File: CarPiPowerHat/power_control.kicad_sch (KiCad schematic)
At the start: 21 parts, among them U3 LM3480-5.0, U4 ATtiny45V-10X

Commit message: updated layout
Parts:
- D5: footprint Diode_SMD:D_0603_1608Metric_Pad1.05x0.95mm_HandSolder -> Diode_SMD:D_SMA_Handsoldering
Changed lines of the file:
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@@
-(kicad_sch (version 20210126) (generator eeschema)
+(kicad_sch (version 20210406) (generator eeschema)
   (paper "A4")
   (junction (at 41.91 43.815) (diameter 1.016) (color 0 0 0 0))
@@
       (effects (font (size 1.27 1.27)) (justify right))
     )
-    (property "Footprint" "Diode_SMD:D_0603_1608Metric_Pad1.05x0.95mm_HandSolder" (id 2) (at 41.91 50.165 0)
-      (effects (font (size 1.27 1.27)) hide)
-    )
+    (property "Footprint" "Diode_SMD:D_SMA_Handsoldering" (id 2) (at 41.91 50.165 0)
+      (effects (font (size 1.27 1.27)) hide)
+    )

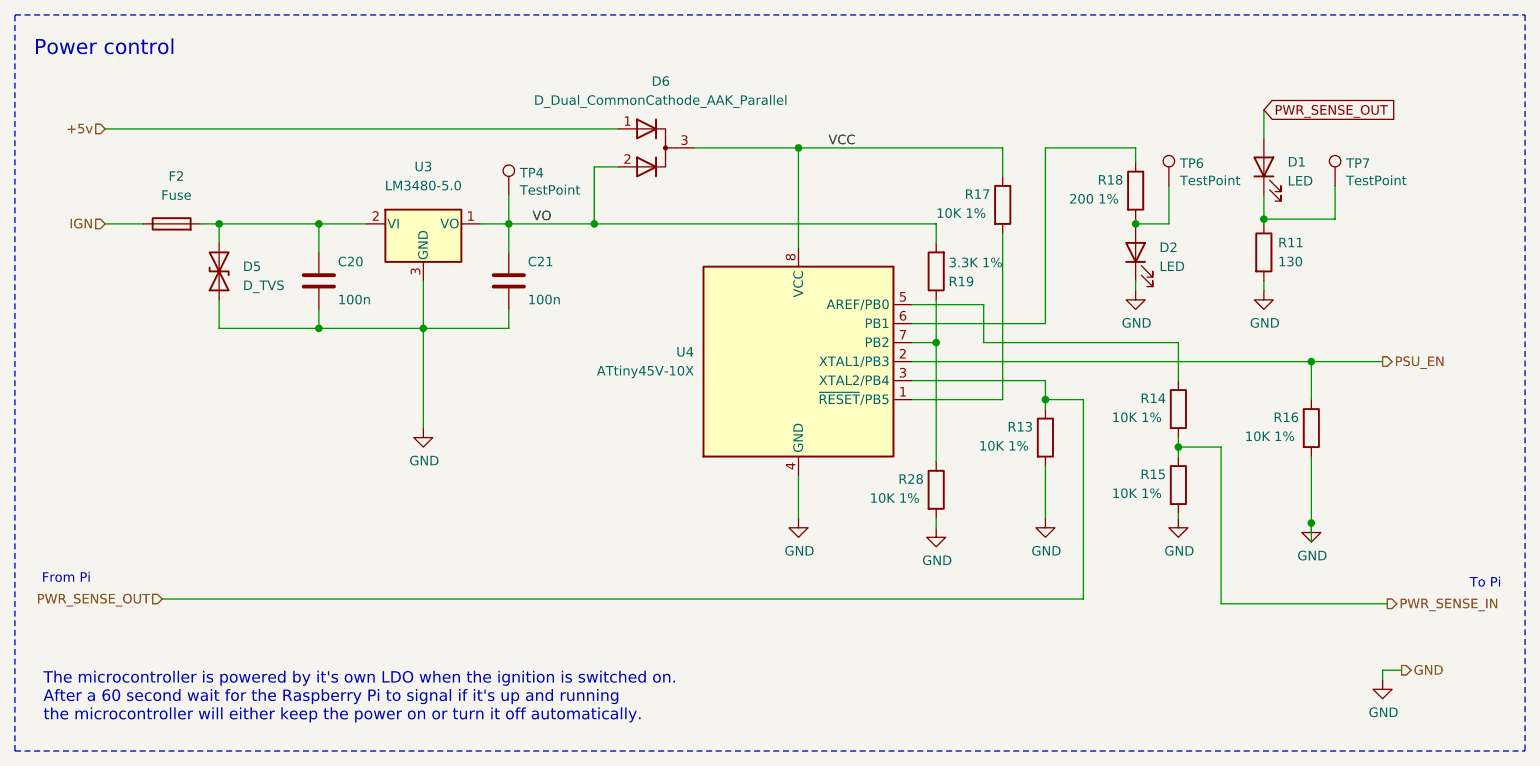
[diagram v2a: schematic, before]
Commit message: Removed TVS diodes for now, fixed DRC issues
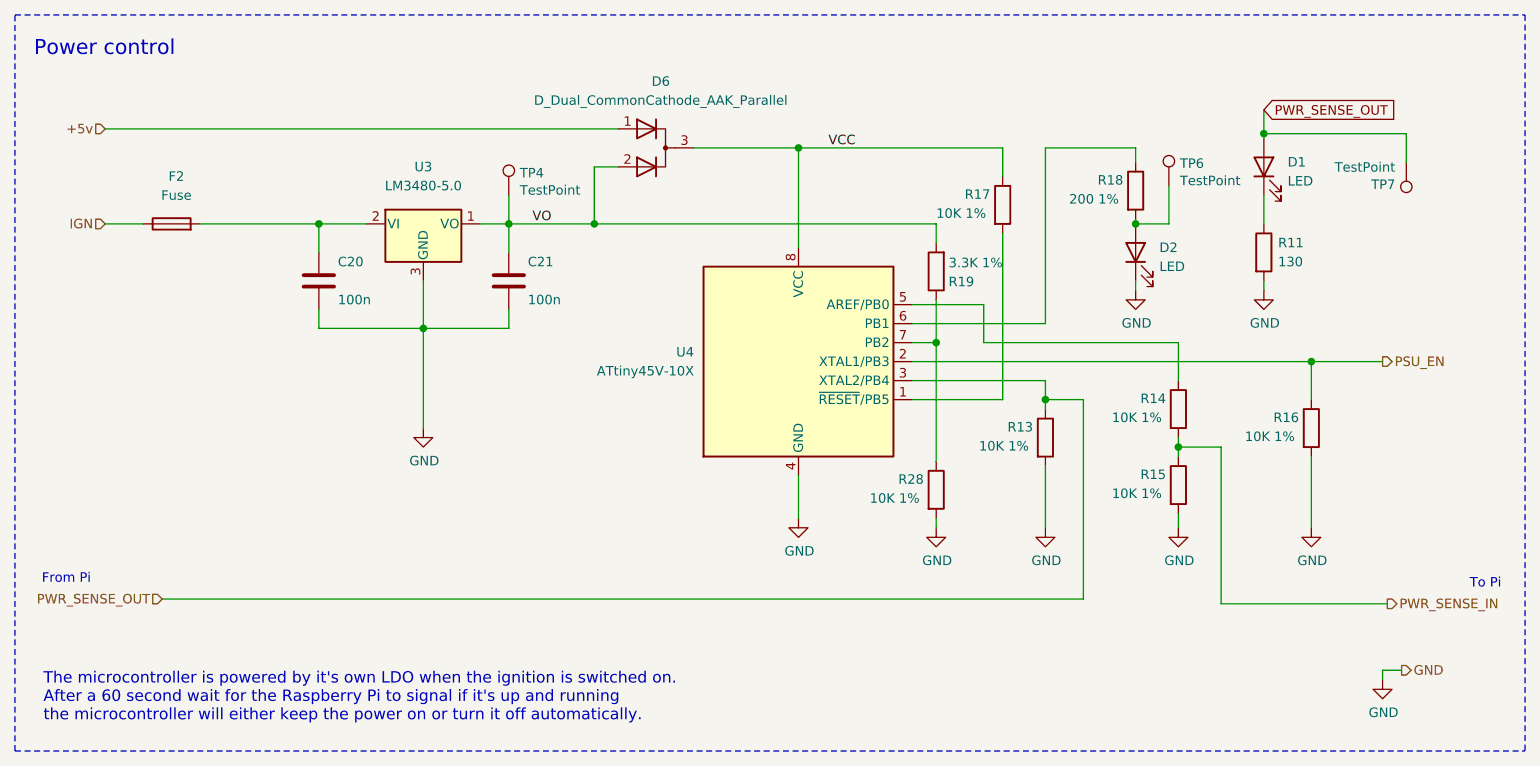
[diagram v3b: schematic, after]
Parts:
- removed D5: D_TVS, Diode_SMD:D_SMA_Handsoldering, symbol Device:D_TVS
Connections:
- net PWR_SENSE_OUT: now also TP7.1
- net at D1.1 (K), R11.1: no longer TP7.1
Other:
- moved on the sheet: TP7
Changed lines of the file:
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@@
 (kicad_sch (version 20210621) (generator eeschema)
   (paper "A4")
-  (junction (at 41.91 43.815) (diameter 1.016) (color 0 0 0 0))
   (junction (at 55.245 43.815) (diameter 1.016) (color 0 0 0 0))
-  (junction (at 55.245 57.785) (diameter 1.016) (color 0 0 0 0))
   (junction (at 69.215 57.785) (diameter 1.016) (color 0 0 0 0))
   (junction (at 80.645 43.815) (diameter 1.016) (color 0 0 0 0))
@@
   (junction (at 164.465 43.815) (diameter 1.016) (color 0 0 0 0))
   (junction (at 170.18 73.66) (diameter 1.016) (color 0 0 0 0))
-  (junction (at 181.61 43.18) (diameter 1.016) (color 0 0 0 0))
+  (junction (at 181.61 31.75) (diameter 1.016) (color 0 0 0 0))
   (junction (at 187.96 62.23) (diameter 1.016) (color 0 0 0 0))
-  (junction (at 187.96 83.82) (diameter 1.016) (color 0 0 0 0))
   (wire (pts (xy 26.67 31.115) (xy 95.25 31.115))
     (stroke (width 0) (type solid) (color 0 0 0 0))
@@
     (stroke (width 0) (type solid) (color 0 0 0 0))
   )
-  (wire (pts (xy 39.37 43.815) (xy 41.91 43.815))
-    (stroke (width 0) (type solid) (color 0 0 0 0))
-  )
-  (wire (pts (xy 41.91 43.815) (xy 41.91 46.355))
-    (stroke (width 0) (type solid) (color 0 0 0 0))
-  )
-  (wire (pts (xy 41.91 43.815) (xy 55.245 43.815))
-    (stroke (width 0) (type solid) (color 0 0 0 0))
-  )
-  (wire (pts (xy 41.91 53.975) (xy 41.91 57.785))
-    (stroke (width 0) (type solid) (color 0 0 0 0))
-  )
-  (wire (pts (xy 41.91 57.785) (xy 55.245 57.785))
+  (wire (pts (xy 39.37 43.815) (xy 55.245 43.815))
     (stroke (width 0) (type solid) (color 0 0 0 0))
   )
@@
     (stroke (width 0) (type solid) (color 0 0 0 0))
   )
-  (wire (pts (xy 152.4 76.2) (xy 152.4 83.185))
+  (wire (pts (xy 152.4 76.2) (xy 152.4 84.455))
     (stroke (width 0) (type solid) (color 0 0 0 0))
   )
@@
     (stroke (width 0) (type solid) (color 0 0 0 0))
   )
-  (wire (pts (xy 170.18 82.55) (xy 170.18 83.185))
+  (wire (pts (xy 170.18 82.55) (xy 170.18 84.455))
     (stroke (width 0) (type solid) (color 0 0 0 0))
   )
@@
     (stroke (width 0) (type solid) (color 0 0 0 0))
   )
-  (wire (pts (xy 181.61 28.575) (xy 181.61 32.385))
-    (stroke (width 0) (type solid) (color 0 0 0 0))
-  )
-  (wire (pts (xy 181.61 40.005) (xy 181.61 43.18))
-    (stroke (width 0) (type solid) (color 0 0 0 0))
-  )
-  (wire (pts (xy 181.61 43.18) (xy 181.61 43.815))
+  (wire (pts (xy 181.61 28.575) (xy 181.61 31.75))
+    (stroke (width 0) (type solid) (color 0 0 0 0))
+  )
+  (wire (pts (xy 181.61 31.75) (xy 181.61 32.385))
+    (stroke (width 0) (type solid) (color 0 0 0 0))
+  )
+  (wire (pts (xy 181.61 31.75) (xy 200.66 31.75))
+    (stroke (width 0) (type solid) (color 0 0 0 0))
+  )
+  (wire (pts (xy 181.61 40.005) (xy 181.61 43.815))
     (stroke (width 0) (type solid) (color 0 0 0 0))
   )
@@
     (stroke (width 0) (type solid) (color 0 0 0 0))
   )
-  (wire (pts (xy 187.96 74.93) (xy 187.96 83.82))
-    (stroke (width 0) (type solid) (color 0 0 0 0))
-  )
-  (wire (pts (xy 187.96 86.36) (xy 187.96 83.82))
-    (stroke (width 0) (type solid) (color 0 0 0 0))
-  )
-  (wire (pts (xy 191.135 38.735) (xy 191.135 43.18))
-    (stroke (width 0) (type solid) (color 0 0 0 0))
-  )
-  (wire (pts (xy 191.135 43.18) (xy 181.61 43.18))
+  (wire (pts (xy 187.96 74.93) (xy 187.96 84.455))
     (stroke (width 0) (type solid) (color 0 0 0 0))
   )
@@
   )
   (wire (pts (xy 200.025 103.505) (xy 197.485 103.505))
+    (stroke (width 0) (type solid) (color 0 0 0 0))
+  )
+  (wire (pts (xy 200.66 31.75) (xy 200.66 35.56))
     (stroke (width 0) (type solid) (color 0 0 0 0))
   )
@@
     (pin "1")
   )
-  (symbol (lib_id "Connector:TestPoint") (at 191.135 38.735 0) (unit 1)
-    (in_bom yes) (on_board yes)
-    (property "Reference" "TP7" (id 0) (at 192.6082 35.7378 0)
-      (effects (font (size 1.27 1.27)) (justify left))
-    )
-    (property "Value" "TestPoint" (id 1) (at 192.6082 38.0492 0)
-      (effects (font (size 1.27 1.27)) (justify left))
-    )
-    (property "Footprint" "TestPoint:TestPoint_Pad_2.0x2.0mm" (id 2) (at 196.215 38.735 0)
-      (effects (font (size 1.27 1.27)) hide)
-    )
-    (property "Datasheet" "~" (id 3) (at 196.215 38.735 0)
-      (effects (font (size 1.27 1.27)) hide)
-    )
-    (property "Field4" "nf" (id 4) (at 191.135 38.735 0)
-      (effects (font (size 1.27 1.27)) hide)
-    )
-    (property "Field5" "nf" (id 5) (at 191.135 38.735 0)
-      (effects (font (size 1.27 1.27)) hide)
-    )
-    (property "Field6" "nf" (id 6) (at 191.135 38.735 0)
-      (effects (font (size 1.27 1.27)) hide)
-    )
-    (property "Field7" "nf" (id 7) (at 191.135 38.735 0)
+  (symbol (lib_id "Connector:TestPoint") (at 200.66 35.56 180) (unit 1)
+    (in_bom yes) (on_board yes)
+    (property "Reference" "TP7" (id 0) (at 199.1868 38.5572 0)
+      (effects (font (size 1.27 1.27)) (justify left))
+    )
+    (property "Value" "TestPoint" (id 1) (at 199.1868 36.2458 0)
+      (effects (font (size 1.27 1.27)) (justify left))
+    )
+    (property "Footprint" "TestPoint:TestPoint_Pad_2.0x2.0mm" (id 2) (at 195.58 35.56 0)
+      (effects (font (size 1.27 1.27)) hide)
+    )
+    (property "Datasheet" "~" (id 3) (at 195.58 35.56 0)
+      (effects (font (size 1.27 1.27)) hide)
+    )
+    (property "Field4" "nf" (id 4) (at 200.66 35.56 0)
+      (effects (font (size 1.27 1.27)) hide)
+    )
+    (property "Field5" "nf" (id 5) (at 200.66 35.56 0)
+      (effects (font (size 1.27 1.27)) hide)
+    )
+    (property "Field6" "nf" (id 6) (at 200.66 35.56 0)
+      (effects (font (size 1.27 1.27)) hide)
+    )
+    (property "Field7" "nf" (id 7) (at 200.66 35.56 0)
       (effects (font (size 1.27 1.27)) hide)
     )
@@
     (pin "1")
   )
-  (symbol (lib_id "power:GND") (at 152.4 83.185 0) (unit 1)
-    (in_bom yes) (on_board yes)
-    (property "Reference" "#PWR0117" (id 0) (at 152.4 89.535 0)
-      (effects (font (size 1.27 1.27)) hide)
-    )
-    (property "Value" "GND" (id 1) (at 152.527 87.5792 0))
-    (property "Footprint" "" (id 2) (at 152.4 83.185 0)
-      (effects (font (size 1.27 1.27)) hide)
-    )
-    (property "Datasheet" "" (id 3) (at 152.4 83.185 0)
+  (symbol (lib_id "power:GND") (at 152.4 84.455 0) (unit 1)
+    (in_bom yes) (on_board yes)
+    (property "Reference" "#PWR0117" (id 0) (at 152.4 90.805 0)
+      (effects (font (size 1.27 1.27)) hide)
+    )
+    (property "Value" "GND" (id 1) (at 152.527 88.8492 0))
+    (property "Footprint" "" (id 2) (at 152.4 84.455 0)
+      (effects (font (size 1.27 1.27)) hide)
+    )
+    (property "Datasheet" "" (id 3) (at 152.4 84.455 0)
       (effects (font (size 1.27 1.27)) hide)
     )
@@
     (pin "1")
   )
-  (symbol (lib_id "power:GND") (at 170.18 83.185 0) (unit 1)
-    (in_bom yes) (on_board yes)
-    (property "Reference" "#PWR0116" (id 0) (at 170.18 89.535 0)
-      (effects (font (size 1.27 1.27)) hide)
-    )
-    (property "Value" "GND" (id 1) (at 170.307 87.5792 0))
-    (property "Footprint" "" (id 2) (at 170.18 83.185 0)
-      (effects (font (size 1.27 1.27)) hide)
-    )
-    (property "Datasheet" "" (id 3) (at 170.18 83.185 0)
+  (symbol (lib_id "power:GND") (at 170.18 84.455 0) (unit 1)
+    (in_bom yes) (on_board yes)
+    (property "Reference" "#PWR0116" (id 0) (at 170.18 90.805 0)
+      (effects (font (size 1.27 1.27)) hide)
+    )
+    (property "Value" "GND" (id 1) (at 170.307 88.8492 0))
+    (property "Footprint" "" (id 2) (at 170.18 84.455 0)
+      (effects (font (size 1.27 1.27)) hide)
+    )
+    (property "Datasheet" "" (id 3) (at 170.18 84.455 0)
       (effects (font (size 1.27 1.27)) hide)
     )
@@
     (pin "1")
   )
-  (symbol (lib_id "power:GND") (at 187.96 83.82 0) (unit 1)
-    (in_bom yes) (on_board yes)
-    (property "Reference" "#PWR0115" (id 0) (at 187.96 90.17 0)
-      (effects (font (size 1.27 1.27)) hide)
-    )
-    (property "Value" "GND" (id 1) (at 188.087 88.2142 0))
-    (property "Footprint" "" (id 2) (at 187.96 83.82 0)
-      (effects (font (size 1.27 1.27)) hide)
-    )
-    (property "Datasheet" "" (id 3) (at 187.96 83.82 0)
+  (symbol (lib_id "power:GND") (at 187.96 84.455 0) (unit 1)
+    (in_bom yes) (on_board yes)
+    (property "Reference" "#PWR0115" (id 0) (at 187.96 90.805 0)
+      (effects (font (size 1.27 1.27)) hide)
+    )
+    (property "Value" "GND" (id 1) (at 188.087 88.8492 0))
+    (property "Footprint" "" (id 2) (at 187.96 84.455 0)
+      (effects (font (size 1.27 1.27)) hide)
+    )
+    (property "Datasheet" "" (id 3) (at 187.96 84.455 0)
       (effects (font (size 1.27 1.27)) hide)
     )
@@
       (effects (font (size 1.27 1.27)) hide)
     )
-    (pin "1")
-    (pin "2")
-  )
-  (symbol (lib_id "Device:D_TVS") (at 41.91 50.165 90) (unit 1)
-    (in_bom yes) (on_board yes)
-    (property "Reference" "D5" (id 0) (at 45.085 49.53 90)
-      (effects (font (size 1.27 1.27)) (justify right))
-    )
-    (property "Value" "D_TVS" (id 1) (at 45.085 52.07 90)
-      (effects (font (size 1.27 1.27)) (justify right))
-    )
-    (property "Footprint" "Diode_SMD:D_SMA_Handsoldering" (id 2) (at 41.91 50.165 0)
-      (effects (font (size 1.27 1.27)) hide)
-    )
-    (property "Datasheet" "~" (id 3) (at 41.91 50.165 0)
-      (effects (font (size 1.27 1.27)) hide)
-    )

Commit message: Finished Layout
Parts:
- removed D6: D_Dual_CommonCathode_AAK_Parallel, Package_TO_SOT_SMD:SOT-23, symbol Device:D_Dual_CommonCathode_AAK_Parallel
- added D6: BAT54C-7-F, Package_TO_SOT_SMD:SOT-23, symbol Diode:BAT54C
- D1: value LED -> LED Red
- D2: value LED -> LED Green
- R11: footprint Resistor_SMD:R_0603_1608Metric -> Resistor_SMD:R_0402_1005Metric; LCSC C22796 -> (none)
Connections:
- net +5v: now also D6.2
- net VCC: now also D6.3
- net VO: now also D6.1
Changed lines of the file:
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@@
   (junction (at 69.215 57.785) (diameter 1.016) (color 0 0 0 0))
   (junction (at 80.645 43.815) (diameter 1.016) (color 0 0 0 0))
-  (junction (at 92.075 43.815) (diameter 1.016) (color 0 0 0 0))
+  (junction (at 100.33 43.815) (diameter 1.016) (color 0 0 0 0))
   (junction (at 119.38 33.655) (diameter 1.016) (color 0 0 0 0))
   (junction (at 137.795 59.69) (diameter 1.016) (color 0 0 0 0))
@@
   (junction (at 181.61 31.75) (diameter 1.016) (color 0 0 0 0))
   (junction (at 187.96 62.23) (diameter 1.016) (color 0 0 0 0))
-  (wire (pts (xy 26.67 31.115) (xy 95.25 31.115))
-    (stroke (width 0) (type solid) (color 0 0 0 0))
-  )
   (wire (pts (xy 26.67 43.815) (xy 31.75 43.815))
     (stroke (width 0) (type solid) (color 0 0 0 0))
   )
+  (wire (pts (xy 28.575 26.035) (xy 100.33 26.035))
+    (stroke (width 0) (type solid) (color 0 0 0 0))
+  )
   (wire (pts (xy 34.29 93.98) (xy 157.48 93.98))
     (stroke (width 0) (type solid) (color 0 0 0 0))
@@
     (stroke (width 0) (type solid) (color 0 0 0 0))
   )
-  (wire (pts (xy 80.645 43.815) (xy 92.075 43.815))
+  (wire (pts (xy 80.645 43.815) (xy 100.33 43.815))
     (stroke (width 0) (type solid) (color 0 0 0 0))
   )
@@
     (stroke (width 0) (type solid) (color 0 0 0 0))
   )
-  (wire (pts (xy 92.075 36.195) (xy 95.25 36.195))
-    (stroke (width 0) (type solid) (color 0 0 0 0))
-  )
-  (wire (pts (xy 92.075 43.815) (xy 92.075 36.195))
-    (stroke (width 0) (type solid) (color 0 0 0 0))
-  )
-  (wire (pts (xy 92.075 43.815) (xy 137.795 43.815))
+  (wire (pts (xy 100.33 41.275) (xy 100.33 43.815))
+    (stroke (width 0) (type solid) (color 0 0 0 0))
+  )
+  (wire (pts (xy 100.33 43.815) (xy 137.795 43.815))
     (stroke (width 0) (type solid) (color 0 0 0 0))
   )
@@
     )
   )
-  (hierarchical_label "+5v" (shape input) (at 26.67 31.115 180)
+  (hierarchical_label "IGN" (shape input) (at 26.67 43.815 180)
     (effects (font (size 1.27 1.27)) (justify right))
   )
-  (hierarchical_label "IGN" (shape input) (at 26.67 43.815 180)
+  (hierarchical_label "+5v" (shape input) (at 28.575 26.035 180)
     (effects (font (size 1.27 1.27)) (justify right))
   )
@@
       (effects (font (size 1.27 1.27)) (justify left))
     )
-    (property "Footprint" "Resistor_SMD:R_0603_1608Metric" (id 2) (at 179.832 47.625 90)
+    (property "Footprint" "Resistor_SMD:R_0402_1005Metric" (id 2) (at 179.832 47.625 90)
       (effects (font (size 1.27 1.27)) hide)
     )
@@
       (effects (font (size 1.27 1.27)) hide)
     )
-    (property "LCSC" "C22796" (id 4) (at 181.61 47.625 0)
+    (property "LCSC" "" (id 4) (at 181.61 47.625 0)
       (effects (font (size 1.27 1.27)) hide)
     )
@@
       (effects (font (size 1.27 1.27)) (justify right))
     )
-    (property "Value" "LED" (id 1) (at 167.64 49.53 90)
+    (property "Value" "LED Green" (id 1) (at 167.64 49.53 90)
       (effects (font (size 1.27 1.27)) (justify right))
     )
@@
       (effects (font (size 1.27 1.27)) (justify right))
     )
-    (property "Value" "LED" (id 1) (at 184.785 38.1 90)
+    (property "Value" "LED Red" (id 1) (at 184.785 38.1 90)
       (effects (font (size 1.27 1.27)) (justify right))
     )
@@
     (pin "2")
   )
-  (symbol (lib_id "Device:D_Dual_CommonCathode_AAK_Parallel") (at 100.33 33.655 0) (unit 1)
-    (in_bom yes) (on_board yes)
-    (property "Reference" "D6" (id 0) (at 100.965 24.765 0))
-    (property "Value" "D_Dual_CommonCathode_AAK_Parallel" (id 1) (at 100.965 27.305 0))
-    (property "Footprint" "Package_TO_SOT_SMD:SOT-23" (id 2) (at 101.6 33.655 0)
-      (effects (font (size 1.27 1.27)) hide)
-    )
-    (property "Datasheet" "~" (id 3) (at 101.6 33.655 0)
-      (effects (font (size 1.27 1.27)) hide)
-    )
-    (property "LCSC" "C68978" (id 4) (at 100.33 33.655 0)
-      (effects (font (size 1.27 1.27)) hide)
-    )
+  (symbol (lib_id "Diode:BAT54C") (at 100.33 33.655 90) (unit 1)
+    (in_bom yes) (on_board yes)
+    (property "Reference" "D6" (id 0) (at 98.1202 32.512 90)
+      (effects (font (size 1.27 1.27)) (justify left))
+    )
+    (property "Value" "BAT54C-7-F" (id 1) (at 98.1202 34.798 90)
+      (effects (font (size 1.27 1.27)) (justify left))
+    )
+    (property "Footprint" "Package_TO_SOT_SMD:SOT-23" (id 2) (at 97.155 31.75 0)
+      (effects (font (size 1.27 1.27)) (justify left) hide)
+    )
+    (property "Datasheet" "http://www.farnell.com/datasheets/2861240.pdf?_ga=2.129831176.54358802.1587372871-1787849031.1568210898&_gac=1.175311126.1587399424.EAIaIQobChMInOvF07P36AIVw7HtCh0NWwCeEAAYAyAAEgI0YfD_BwE" (id 3) (at 100.33 35.687 0)
+      (effects (font (size 1.27 1.27)) hide)
+    )
+    (property "Field4" "Farnell" (id 4) (at 100.33 33.655 0)
+      (effects (font (size 1.27 1.27)) hide)
+    )
+    (property "Field5" "2306010" (id 5) (at 100.33 33.655 0)
+      (effects (font (size 1.27 1.27)) hide)
+    )
+    (property "Field6" "BAT54C-7-F" (id 6) (at 100.33 33.655 0)
+      (effects (font (size 1.27 1.27)) hide)
+    )
+    (property "Field7" "Rohm" (id 7) (at 100.33 33.655 0)
+      (effects (font (size 1.27 1.27)) hide)
+    )
+    (property "Part Description" "Diode Array 1 Pair Common Cathode Schottky 30V 200mA (DC) Surface Mount TO-236-3, SC-59, SOT-23-3" (id 8) (at 100.33 33.655 0)
+      (effects (font (size 1.27 1.27)) hide)
+    )
+    (property "LCSC" "C37704" (id 9) (at 100.33 33.655 90)
+      (effects (font (size 1.27 1.27)) hide)
+    )
